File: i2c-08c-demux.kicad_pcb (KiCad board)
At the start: 2 copper layers, 14.2 x 30.5 mm, 15 parts, among them J1 Conn_01x05, J3 Conn_01x04, J4 Conn_01x04, Q1 NMOS, Q2 NMOS, Q3 NMOS, Q4 NMOS, Q5 NMOS, Q6 NMOS, Q7 NMOS, Q8 NMOS, U1 TCA9554DWT

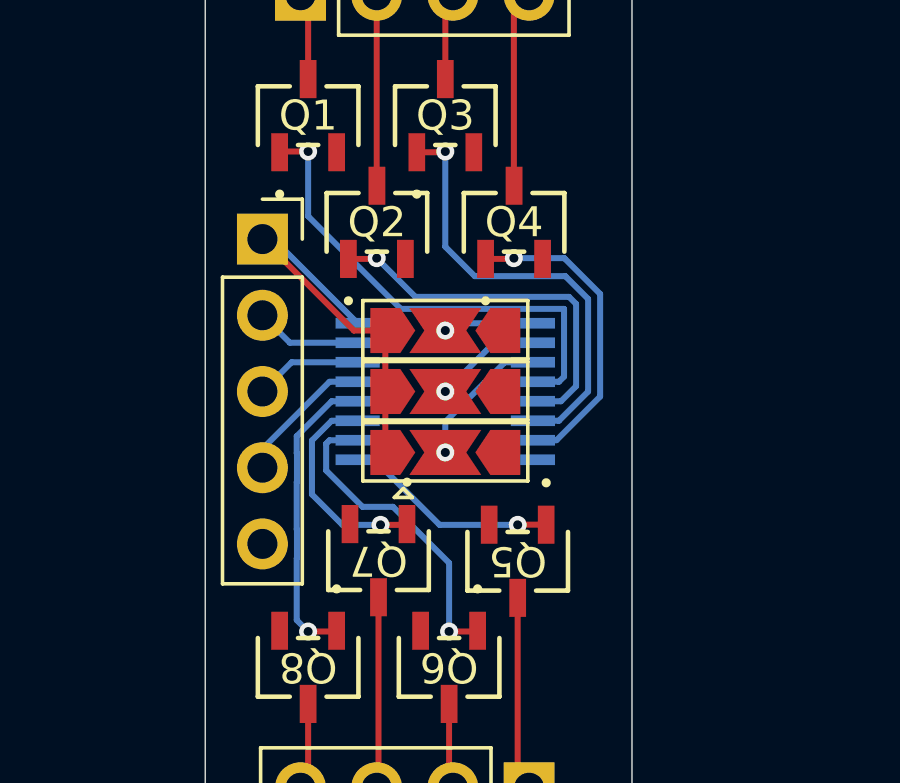
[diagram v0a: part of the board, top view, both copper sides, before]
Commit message: pcb masked
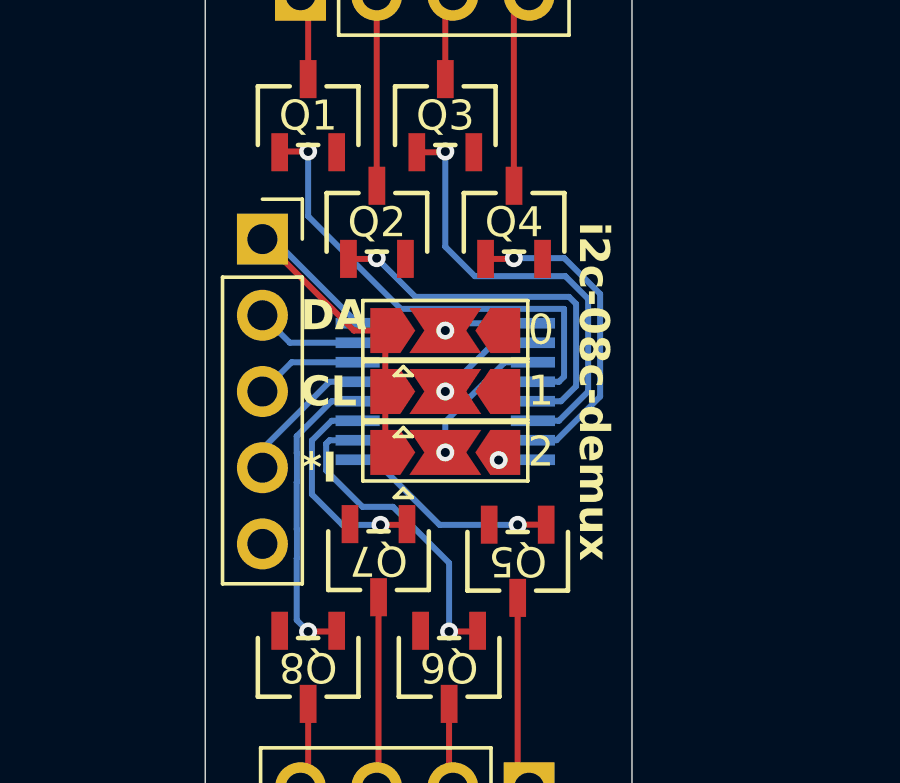
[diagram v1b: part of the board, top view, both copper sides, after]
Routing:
- net GND: track 0.00 -> 1.13 mm, vias 0 -> 1
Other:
- board text added: "*I"
- board text added: "0"
- board text added: "1"
- board text added: "2"
- board text added: "CL"
- board text added: "DA"
- board text added: "GND"
- board text added: "VCC"
- board text added: "i2c-08c-demux"
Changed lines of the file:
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@@
 			(layer "F.SilkS")
 		)
-		(fp_circle
-			(center -0.95 2.6162)
-			(end -0.8738 2.6162)
-			(stroke
-				(width 0.1524)
-				(type solid)
-			)
-			(fill no)
-			(layer "F.SilkS")
-		)
 		(fp_line
 			(start -1.8034 -1.1049)
@@
 			(layer "F.SilkS")
 		)
-		(fp_circle
-			(center -0.95 2.6162)
-			(end -0.8738 2.6162)
-			(stroke
-				(width 0.1524)
-				(type solid)
-			)
-			(fill no)
-			(layer "F.SilkS")
-		)
 		(fp_line
 			(start -1.8034 -1.1049)
@@
 			(layer "F.SilkS")
 		)
-		(fp_circle
-			(center -0.95 2.6162)
-			(end -0.8738 2.6162)
-			(stroke
-				(width 0.1524)
-				(type solid)
-			)
-			(fill no)
-			(layer "F.SilkS")
-		)
 		(fp_line
 			(start 1.8034 1.1049)
@@
 			(layer "F.SilkS")
 		)
-		(fp_circle
-			(center -0.95 2.6162)
-			(end -0.8738 2.6162)
-			(stroke
-				(width 0.1524)
-				(type solid)
-			)
-			(fill no)
-			(layer "F.SilkS")
-		)
 		(fp_line
 			(start -1.8034 -1.1049)
@@
 			(layer "F.SilkS")
 		)
-		(fp_circle
-			(center -0.95 2.6162)
-			(end -0.8738 2.6162)
-			(stroke
-				(width 0.1524)
-				(type solid)
-			)
-			(fill no)
-			(layer "F.SilkS")
-		)
 		(fp_line
 			(start 1.8034 1.1049)
@@
 			(layer "F.SilkS")
 		)
-		(fp_circle
-			(center -0.95 2.6162)
-			(end -0.8738 2.6162)
-			(stroke
-				(width 0.1524)
-				(type solid)
-			)
-			(fill no)
-			(layer "F.SilkS")
-		)
 		(fp_line
 			(start 1.8034 1.1049)
@@
 		)
 		(fp_line
+			(start -1.7 1.5)
+			(end -1.1 1.5)
+			(stroke
+				(width 0.12)
+				(type solid)
+			)
+			(layer "F.SilkS")
+		)
+		(fp_line
+			(start -1.4 1.2)
+			(end -1.7 1.5)
+			(stroke
+				(width 0.12)
+				(type solid)
+			)
+			(layer "F.SilkS")
+		)
+		(fp_line
+			(start -1.1 1.5)
+			(end -1.4 1.2)
+			(stroke
+				(width 0.12)
+				(type solid)
+			)
+			(layer "F.SilkS")
+		)
+		(fp_line
 			(start 2.75 -1)
 			(end 2.75 0.95)
@@
 		)
 		(fp_line
+			(start -1.7 1.5)
+			(end -1.1 1.5)
+			(stroke
+				(width 0.12)
+				(type solid)
+			)
+			(layer "F.SilkS")
+		)
+		(fp_line
+			(start -1.4 1.2)
+			(end -1.7 1.5)
+			(stroke
+				(width 0.12)
+				(type solid)
+			)
+			(layer "F.SilkS")
+		)
+		(fp_line
+			(start -1.1 1.5)
+			(end -1.4 1.2)
+			(stroke
+				(width 0.12)
+				(type solid)
+			)
+			(layer "F.SilkS")
+		)
+		(fp_line
 			(start 2.75 -1)
 			(end 2.75 0.95)
@@
 			(layer "F.SilkS")
 		)
-		(fp_circle
-			(center -0.95 2.6162)
-			(end -0.8738 2.6162)
-			(stroke
-				(width 0.1524)
-				(type solid)
-			)
-			(fill no)
-			(layer "F.SilkS")
-		)
 		(fp_line
 			(start -1.8034 -1.1049)
@@
 			(layer "F.SilkS")
 		)
-		(fp_circle
-			(center -0.95 2.6162)
-			(end -0.8738 2.6162)
-			(stroke
-				(width 0.1524)
-				(type solid)
-			)
-			(fill no)
-			(layer "F.SilkS")
-		)
 		(fp_line
 			(start 1.8034 1.1049)
@@
 			(layer "B.Fab")
 		)
-		(fp_text user "${REFERENCE}"
-			(at 0 0 0)
+		(fp_text user "*"
+			(at -3.175 3.773601 0)
+			(layer "B.SilkS")
+			(effects
+				(font
+					(size 1 1)
+					(thickness 0.15)
+				)
+				(justify mirror)
+			)
+		)
+		(fp_text user "*"
+			(at -3.175 3.773601 0)
 			(unlocked yes)
-			(layer "B.Fab")
+			(layer "B.SilkS")
 			(effects
 				(font
@@
 			)
 		)
+		(fp_text user "${REFERENCE}"
+			(at 0 0 0)
+			(unlocked yes)
+			(layer "B.Fab")
+			(effects
+				(font
+					(size 1 1)
+					(thickness 0.15)
+				)
+				(justify mirror)
+			)
+		)
 		(fp_text user "*"
 			(at -1.8669 2.4765 0)
@@
 		(layer "Edge.Cuts")
 	)
+	(gr_text "DA"
+		(at 104.775 88.9 0)
+		(layer "F.SilkS")
+		(effects
+			(font
+				(size 1 1)
+				(thickness 0.2)
+				(bold yes)
+			)
+			(justify left)
+		)
+	)
+	(gr_text "2"
+		(at 112.351 93.447 0)
+		(layer "F.SilkS")
+		(effects
+			(font
+				(size 1 1)
+				(thickness 0.125)
+			)
+			(justify left)
+		)
+	)
+	(gr_text "1"
+		(at 112.351 91.415 0)
+		(layer "F.SilkS")
+		(effects
+			(font
+				(size 1 1)
+				(thickness 0.125)
+			)
+			(justify left)
+		)
+	)
+	(gr_text "0"
+		(at 112.351 89.383 0)
+		(layer "F.SilkS")
+		(effects
+			(font
+				(size 1 1)
+				(thickness 0.125)
+			)
+			(justify left)
+		)
+	)
+	(gr_text "CL"
+		(at 104.775 91.44 0)
+		(layer "F.SilkS")
+		(effects
+			(font
+				(size 1 1)
+				(thickness 0.2)
+				(bold yes)
+			)
+			(justify left)
+		)
+	)
+	(gr_text "i2c-08c-demux"
+		(at 114.554 91.44 270)
+		(layer "F.SilkS")
+		(effects
+			(font
+				(size 1 1)
+				(thickness 0.2)
+				(bold yes)
+			)
+		)
+	)
+	(gr_text "*I"
+		(at 104.775 93.98 0)
+		(layer "F.SilkS")
+		(effects
+			(font
+				(size 1 1)
+				(thickness 0.2)
+				(bold yes)
+			)
+			(justify left)
+		)
+	)
+	(gr_text "VCC"
+		(at 104.394 86.36 0)
+		(layer "B.SilkS")
+		(effects
+			(font
+				(size 1 1)
+				(thickness 0.2)
+				(bold yes)
+			)
+			(justify right mirror)
+		)
+	)
+	(gr_text "GND"
+		(at 104.394 96.52 0)
+		(layer "B.SilkS")
+		(effects
+			(font
+				(size 1 1)
+				(thickness 0.2)
+				(bold yes)
+			)
+			(justify right mirror)
+		)
+	)
 	(segment
 		(start 103.505 91.44)
@@
 		(net 2)
 	)
+	(via
+		(at 111.379 93.726)
+		(size 0.6)
+		(drill 0.3)
+		(layers "F.Cu" "B.Cu")
+		(net 3)
+	)
+	(segment
+		(start 112.522 93.714999)
+		(end 111.390001 93.714999)
+		(width 0.2)
+		(layer "B.Cu")
+		(net 3)
+	)
 	(segment
 		(start 103.505 93.353402)
@@
 	)
 	(group ""
-		(members "5c99ce76-3657-4298-8372-f200f966df40" "9ebc5bcd-753f-4c0d-9a8c-5a9b0ecdb716"
-			"c1b0b5e2-43ed-47b3-b5b2-ebee0e6fdce1" "fde47495-82ae-4fc3-80eb-4c9c48788daf"
+		(members "0d1c3ee6-29e5-4e62-82c1-3d3db1766260" "0e9f7594-a091-434b-9bc7-14c6b97c72a0"
+			"111d3b8d-5e7e-42e6-addc-4c510a5a3969" "5c99ce76-3657-4298-8372-f200f966df40"
+			"9ebc5bcd-753f-4c0d-9a8c-5a9b0ecdb716" "c1b0b5e2-43ed-47b3-b5b2-ebee0e6fdce1"
+			"c3fcc072-ec12-416c-8c42-feb811d6db39" "d571fde4-910b-4352-bad7-bf2823375a91"
+			"d684a844-b64c-4da1-b8c2-432563bc3bfd" "de8562ed-bf3b-49c1-99cc-43213f5009a9"
+			"fde47495-82ae-4fc3-80eb-4c9c48788daf"
 		)
 	)

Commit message: design checked
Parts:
- moved J4 23.3 mm to (130.2, 89.7), turned to 0 degrees
- moved Q8 21.1 mm to (126.0, 98.2), turned to -90 degrees
- moved J3 19.1 mm to (103.5, 97.3), turned to 180 degrees
- moved Q6 17.8 mm to (126.0, 93.5), turned to -90 degrees
- moved Q1 16.1 mm to (107.6, 98.2), turned to 90 degrees
- moved J1 15.7 mm to (111.8, 99.7), turned to 90 degrees
- moved Q7 15.2 mm to (122.5, 95.8), turned to -90 degrees
- moved Q5 12.0 mm to (122.5, 91.2), turned to -90 degrees
- moved Q3 11.5 mm to (107.6, 93.6), turned to 90 degrees
- moved Q2 10.8 mm to (111.2, 95.9), turned to 90 degrees
- moved JP3 9.27 mm to (118.9, 93.6), turned to 90 degrees
- moved JP2 7.55 mm to (116.8, 93.6), turned to 90 degrees
- moved U1 7.55 mm to (116.8, 93.6), turned to -90 degrees
- moved JP1 6.68 mm to (114.8, 93.6), turned to 90 degrees
- moved Q4 5.55 mm to (111.2, 91.3), turned to 90 degrees
- renumbered A0 to JP1, A1 to JP2, A2 to JP3
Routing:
- net Net-(J4-Pin_1): track 6.49 -> 7.11 mm
- net Net-(J4-Pin_2): track 2.85 -> 3.47 mm
- net Net-(J3-Pin_3): track 2.90 -> 3.50 mm
- net Net-(J3-Pin_4): track 6.56 -> 7.16 mm
- net Net-(J3-Pin_2): track 6.35 -> 6.95 mm
- net Net-(J4-Pin_3): track 6.37 -> 6.95 mm
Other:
- board size 14.2 x 30.5 mm -> 30.5 x 14 mm

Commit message: bored
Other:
- board text added: "ADITYA IYER"
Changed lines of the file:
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@@
-		)
-		(fp_line
-			(start -1.4 1.2)
-			(end -1.7 1.5)
-			(stroke
-				(width 0.12)
-				(type solid)
-			)
-			(layer "F.SilkS")
-		)
-		(fp_line
-			(start -1.1 1.5)
-			(end -1.4 1.2)
-			(stroke
-				(width 0.12)
-				(type solid)
-			)
-			(layer "F.SilkS")
-		)
-		(fp_line
-			(start -1.7 1.5)
-			(end -1.1 1.5)
-			(stroke
-				(width 0.12)
-				(type solid)
-			)
-			(layer "F.SilkS")
 		)
 		(fp_line
@@
 		)
 		(fp_line
-			(start -1.4 1.2)
-			(end -1.7 1.5)
-			(stroke
-				(width 0.12)
-				(type solid)
-			)
-			(layer "F.SilkS")
-		)
-		(fp_line
-			(start -1.1 1.5)
-			(end -1.4 1.2)
-			(stroke
-				(width 0.12)
-				(type solid)
-			)
-			(layer "F.SilkS")
-		)
-		(fp_line
-			(start -1.7 1.5)
-			(end -1.1 1.5)
-			(stroke
-				(width 0.12)
-				(type solid)
-			)
-			(layer "F.SilkS")
-		)
-		(fp_line
 			(start -2.98 -1.27)
 			(end 3 -1.27)
@@
 		(embedded_fonts no)
 	)
+	(gr_line
+		(start 120.523 93.472)
+		(end 120.015 93.472)
+		(stroke
+			(width 0.1)
+			(type default)
+		)
+		(layer "F.SilkS")
+	)
+	(gr_line
+		(start 120.269 93.726)
+		(end 120.523 93.472)
+		(stroke
+			(width 0.1)
+			(type default)
+		)
+		(layer "F.SilkS")
+	)
+	(gr_line
+		(start 120.015 93.472)
+		(end 120.142 93.599)
+		(stroke
+			(width 0.1)
+			(type default)
+		)
+		(layer "F.SilkS")
+	)
+	(gr_line
+		(start 120.015 93.472)
+		(end 120.269 93.726)
+		(stroke
+			(width 0.1)
+			(type default)
+		)
+		(layer "F.SilkS")
+	)
+	(gr_line
+		(start 113.411 93.726)
+		(end 113.157 93.472)
+		(stroke
+			(width 0.1)
+			(type default)
+		)
+		(layer "F.SilkS")
+	)
+	(gr_line
+		(start 113.157 93.472)
+		(end 113.665 93.472)
+		(stroke
+			(width 0.1)
+			(type default)
+		)
+		(layer "F.SilkS")
+	)
+	(gr_line
+		(start 113.665 93.472)
+		(end 113.411 93.726)
+		(stroke
+			(width 0.1)
+			(type default)
+		)
+		(layer "F.SilkS")
+	)
 	(gr_rect
 		(start 101.6 87.63)
@@
 		)
 	)
+	(gr_text "ADITYA IYER"
+		(at 128.905 88.773 0)
+		(layer "B.SilkS")
+		(effects
+			(font
+				(size 1 1)
+				(thickness 0.125)
+			)
+			(justify left mirror)
+		)
+	)

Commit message: Better
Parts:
- added G***: LOGO, footprints:logo, B.Cu at (125.7, 94.0)
- J1: footprint Connector_PinSocket_2.54mm:PinSocket_1x05_P2.54mm_Vertical -> Connector_PinSocket_2.54mm:PinSocket_1x04_P2.54mm_Vertical
- moved J1 1.28 mm to (113.0, 99.8)
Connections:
- J1 pad 4: /INT -> GND
- U1 pad 13: /INT -> unconnected-(U1-*INT-Pad13)
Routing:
- net /INT: track 4.73 -> 0.00 mm
- net GND: track 1.13 -> 3.45 mm
- net VCC: track 13.8 -> 12.8 mm
- net /I2C_SCL: track 3.58 -> 4.11 mm
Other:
- board text added: "adityaiyer2007@gmail.com ADITYA IYER"
- board text removed: "*I"
- board text removed: "ADITYA IYER"

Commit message: branding
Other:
- board text added: "adityaiyer2007@gmail.com STANFORD"
- board text removed: "adityaiyer2007@gmail.com ADITYA IYER"
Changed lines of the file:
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@@
 		)
 	)
-	(gr_text "adityaiyer2007@gmail.com\nADITYA IYER"
+	(gr_text "adityaiyer2007@gmail.com\nSTANFORD"
 		(at 128.905 87.884 0)
 		(layer "B.SilkS")
